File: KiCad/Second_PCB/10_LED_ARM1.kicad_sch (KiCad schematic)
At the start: 11 parts

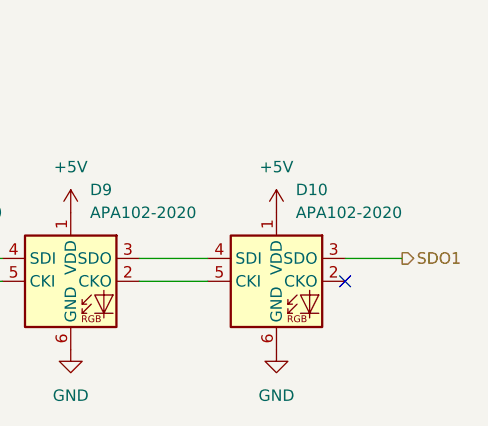
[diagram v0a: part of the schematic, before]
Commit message: added all the kicad files and gerbers of the second pcb
after sending to manufacture.
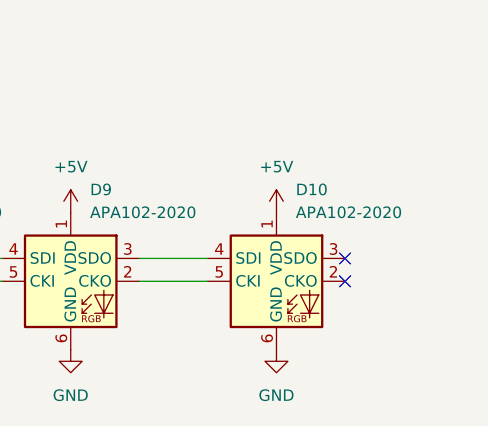
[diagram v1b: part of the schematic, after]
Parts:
- D1, D10, D2, D3, D4, D5, D6, D7, D8, D9: footprint LED_SMD:LED-APA102-2020 -> Spinning_FP:LED-APA102-2020_EDITED
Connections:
- net SDO1: no longer names the net of D10.3 (SDO)
- no-connect marks 1 -> 2
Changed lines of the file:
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@@
+	)
+	(no_connect
+		(at 251.46 64.77)
 	)
 	(no_connect
@@
 	(wire
 		(pts
-			(xy 251.46 64.77) (xy 257.81 64.77)
+			(xy 29.21 67.31) (xy 34.29 67.31)
 		)
 		(stroke
@@
 	(wire
 		(pts
-			(xy 29.21 67.31) (xy 34.29 67.31)
+			(xy 30.48 45.72) (xy 41.91 45.72)
 		)
 		(stroke
@@
 	(wire
 		(pts
-			(xy 30.48 45.72) (xy 41.91 45.72)
+			(xy 207.01 64.77) (xy 213.36 64.77)
 		)
 		(stroke
@@
 	(wire
 		(pts
-			(xy 207.01 64.77) (xy 213.36 64.77)
+			(xy 72.39 67.31) (xy 78.74 67.31)
 		)
 		(stroke
@@
 	(wire
 		(pts
-			(xy 72.39 67.31) (xy 78.74 67.31)
+			(xy 139.7 64.77) (xy 146.05 64.77)
 		)
 		(stroke
@@
 	(wire
 		(pts
-			(xy 139.7 64.77) (xy 146.05 64.77)
+			(xy 161.29 64.77) (xy 168.91 64.77)
 		)
 		(stroke
@@
 	(wire
 		(pts
-			(xy 161.29 64.77) (xy 168.91 64.77)
+			(xy 184.15 64.77) (xy 191.77 64.77)
 		)
 		(stroke
@@
 	(wire
 		(pts
-			(xy 184.15 64.77) (xy 191.77 64.77)
+			(xy 49.53 64.77) (xy 57.15 64.77)
 		)
 		(stroke
@@
 	(wire
 		(pts
-			(xy 49.53 64.77) (xy 57.15 64.77)
+			(xy 49.53 67.31) (xy 57.15 67.31)
 		)
 		(stroke
@@
 	(wire
 		(pts
-			(xy 49.53 67.31) (xy 57.15 67.31)
+			(xy 116.84 67.31) (xy 124.46 67.31)
 		)
 		(stroke
@@
 	(wire
 		(pts
-			(xy 116.84 67.31) (xy 124.46 67.31)
+			(xy 93.98 67.31) (xy 101.6 67.31)
 		)
 		(stroke
@@
 	(wire
 		(pts
-			(xy 93.98 67.31) (xy 101.6 67.31)
+			(xy 184.15 67.31) (xy 191.77 67.31)
 		)
 		(stroke
@@
 	(wire
 		(pts
-			(xy 184.15 67.31) (xy 191.77 67.31)
+			(xy 228.6 64.77) (xy 236.22 64.77)
 		)
 		(stroke
@@
 	(wire
 		(pts
-			(xy 228.6 64.77) (xy 236.22 64.77)
+			(xy 207.01 67.31) (xy 213.36 67.31)
 		)
 		(stroke
@@
 	(wire
 		(pts
-			(xy 207.01 67.31) (xy 213.36 67.31)
+			(xy 116.84 64.77) (xy 124.46 64.77)
 		)
 		(stroke
@@
 	(wire
 		(pts
-			(xy 116.84 64.77) (xy 124.46 64.77)
+			(xy 139.7 67.31) (xy 146.05 67.31)
 		)
 		(stroke
@@
 	(wire
 		(pts
-			(xy 139.7 67.31) (xy 146.05 67.31)
+			(xy 41.91 45.72) (xy 41.91 59.69)
 		)
 		(stroke
@@
 	(wire
 		(pts
-			(xy 41.91 45.72) (xy 41.91 59.69)
+			(xy 41.91 44.45) (xy 41.91 45.72)
 		)
 		(stroke
@@
 	(wire
 		(pts
-			(xy 41.91 44.45) (xy 41.91 45.72)
+			(xy 161.29 67.31) (xy 168.91 67.31)
 		)
 		(stroke
@@
 	(wire
 		(pts
-			(xy 161.29 67.31) (xy 168.91 67.31)
+			(xy 93.98 64.77) (xy 101.6 64.77)
 		)
 		(stroke
 			(width 0)
 			(type default)
-		)
-	)
-	(wire
-		(pts
-			(xy 93.98 64.77) (xy 101.6 64.77)
-		)
-		(stroke
-			(width 0)
-			(type default)
-		)
-	)
-	(hierarchical_label "SDO1"
-		(shape output)
-		(at 257.81 64.77 0)
-		(effects
-			(font
-				(size 1.27 1.27)
-			)
-			(justify left)
 		)
 	)
@@
 			)
 		)
-		(property "Footprint" "LED_SMD:LED-APA102-2020"
+		(property "Footprint" "Spinning_FP:LED-APA102-2020_EDITED"
 			(at 177.8 74.93 0)
 			(effects
@@
 			)
 		)
-		(property "Footprint" "LED_SMD:LED-APA102-2020"
+		(property "Footprint" "Spinning_FP:LED-APA102-2020_EDITED"
 			(at 245.11 74.93 0)
 			(effects
@@
 			)
 		)
-		(property "Footprint" "LED_SMD:LED-APA102-2020"
+		(property "Footprint" "Spinning_FP:LED-APA102-2020_EDITED"
 			(at 43.18 74.93 0)
 			(effects
@@
 			)
 		)
-		(property "Footprint" "LED_SMD:LED-APA102-2020"
+		(property "Footprint" "Spinning_FP:LED-APA102-2020_EDITED"
 			(at 133.35 74.93 0)
 			(effects
@@
 			)
 		)
-		(property "Footprint" "LED_SMD:LED-APA102-2020"
+		(property "Footprint" "Spinning_FP:LED-APA102-2020_EDITED"
 			(at 154.94 74.93 0)
 			(effects
@@
 			)
 		)
-		(property "Footprint" "LED_SMD:LED-APA102-2020"
+		(property "Footprint" "Spinning_FP:LED-APA102-2020_EDITED"
 			(at 222.25 74.93 0)
 			(effects
@@
 			)
 		)
-		(property "Footprint" "LED_SMD:LED-APA102-2020"
+		(property "Footprint" "Spinning_FP:LED-APA102-2020_EDITED"
 			(at 66.04 74.93 0)
 			(effects
@@
 			)
 		)
-		(property "Footprint" "LED_SMD:LED-APA102-2020"
+		(property "Footprint" "Spinning_FP:LED-APA102-2020_EDITED"
 			(at 87.63 74.93 0)
 			(effects
@@
 			)
 		)
-		(property "Footprint" "LED_SMD:LED-APA102-2020"
+		(property "Footprint" "Spinning_FP:LED-APA102-2020_EDITED"
 			(at 110.49 74.93 0)
 			(effects
@@
 			)
 		)
-		(property "Footprint" "LED_SMD:LED-APA102-2020"
+		(property "Footprint" "Spinning_FP:LED-APA102-2020_EDITED"
 			(at 200.66 74.93 0)
 			(effects
